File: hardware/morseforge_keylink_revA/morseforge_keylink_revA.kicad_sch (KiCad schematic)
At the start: 0 parts

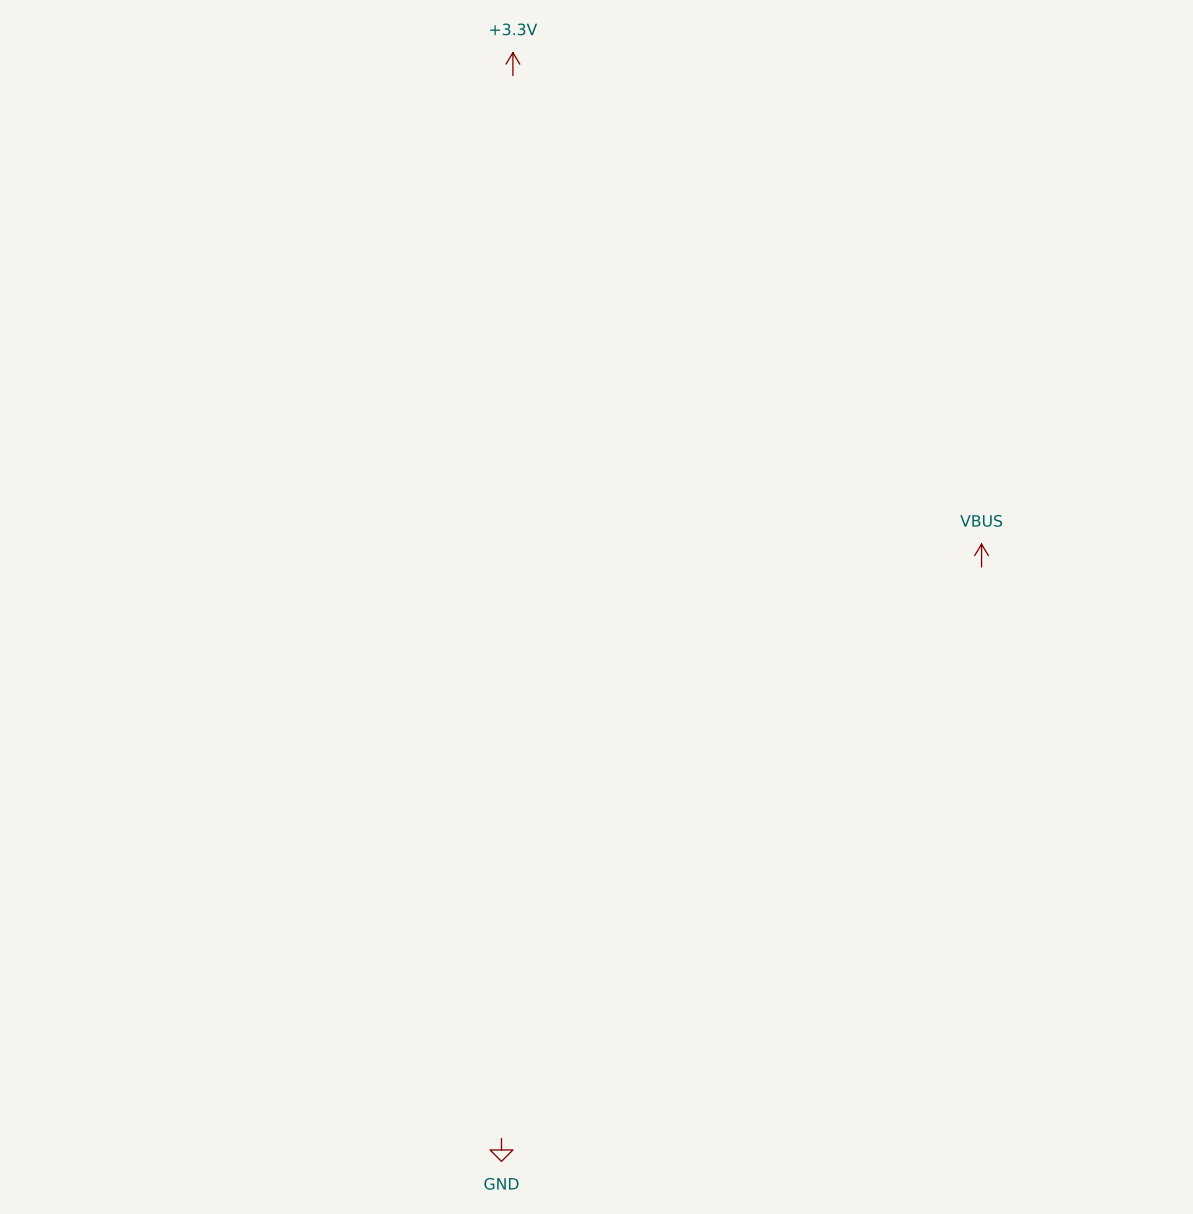
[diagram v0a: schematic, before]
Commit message: PCB schematic USB-C power input block
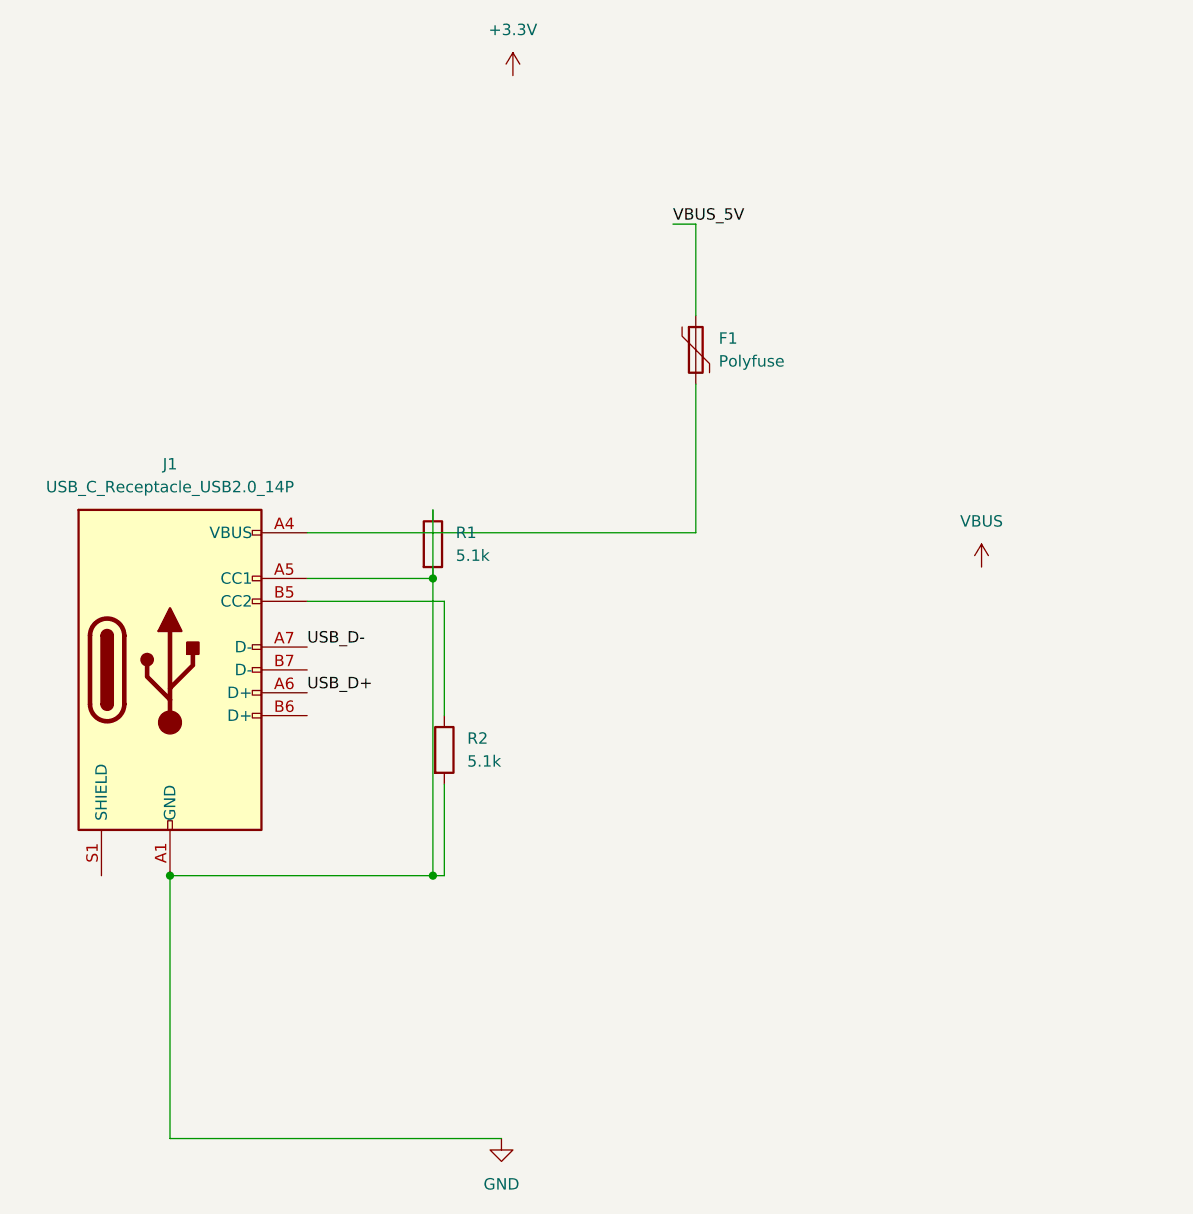
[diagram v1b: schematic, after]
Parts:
- added F1: Polyfuse, symbol Device:Polyfuse
- added J1: USB_C_Receptacle_USB2.0_14P, symbol Connector:USB_C_Receptacle_USB2.0_14P
- added R1, R2: 5.1k, symbol Device:R
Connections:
- net GND: now also J1.A1 (GND), J1.A12 (GND), J1.A5 (CC1), J1.B1 (GND), J1.B12 (GND), R1.1, R1.2, R2.2
- new net: F1.2, J1.A4 (VBUS), J1.A9 (VBUS), J1.B4 (VBUS), J1.B9 (VBUS)
- new net: J1.B5 (CC2), R2.1
- new net USB_D+: J1.A6 (D+)
- new net USB_D-: J1.A7 (D-)
- new net VBUS_5V: F1.1

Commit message: PCB BMS
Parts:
- added C1, C2: 10uF, symbol Device:C
- added D1: LED, symbol Device:LED
- added J2: Conn_01x02_Socket, symbol Connector:Conn_01x02_Socket
- added R3: 5.1k, symbol Device:R
- added R4: 1k, symbol Device:R
- added U1: MCP73831-2-MC, Package_DFN_QFN:DFN-8-1EP_3x2mm_P0.5mm_EP1.7x1.4mm, symbol Battery_Management:MCP73831-2-MC
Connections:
- net GND: now also C1.2, C2.2, J2.2 (Pin_2), R3.2, U1.6 (V_{SS})
- net VBUS_5V: now also C1.1, R4.2, U1.1 (V_{DD}), U1.2 (V_{DD})
- new net: D1.2 (A), R4.1
- new net: R3.1, U1.8 (PROG)
- new net: D1.1 (K), U1.5 (STAT)
- new net: U1.3 (V_{BAT}), U1.4 (V_{BAT})
- new net BAT: C2.1, J2.1 (Pin_1)

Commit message: Fixed wire from BAT to VBAT
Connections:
- net BAT: now also U1.3 (V_{BAT}), U1.4 (V_{BAT})
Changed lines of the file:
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@@
+	)
+	(junction
+		(at 180.34 120.65)
+		(diameter 0)
+		(color 0 0 0 0)
 	)
 	(junction
@@
 	(wire
 		(pts
-			(xy 149.86 120.65) (xy 190.5 120.65)
-		)
-		(stroke
-			(width 0)
-			(type default)
-		)
-	)
-	(wire
-		(pts
 			(xy 152.4 92.71) (xy 162.56 92.71)
 		)
@@
 	(wire
 		(pts
+			(xy 180.34 101.6) (xy 172.72 101.6)
+		)
+		(stroke
+			(width 0)
+			(type default)
+		)
+	)
+	(wire
+		(pts
 			(xy 162.56 92.71) (xy 162.56 96.52)
 		)
@@
 	(wire
 		(pts
+			(xy 180.34 120.65) (xy 190.5 120.65)
+		)
+		(stroke
+			(width 0)
+			(type default)
+		)
+	)
+	(wire
+		(pts
 			(xy 179.07 92.71) (xy 179.07 86.36)
 		)
@@
 	(wire
 		(pts
+			(xy 149.86 120.65) (xy 180.34 120.65)
+		)
+		(stroke
+			(width 0)
+			(type default)
+		)
+	)
+	(wire
+		(pts
 			(xy 105.41 125.73) (xy 134.62 125.73)
 		)
@@
 		)
 		(stroke
+			(width 0)
+			(type default)
+		)
+	)
+	(wire
+		(pts
+			(xy 180.34 120.65) (xy 180.34 101.6)
+		)
+		(stroke
